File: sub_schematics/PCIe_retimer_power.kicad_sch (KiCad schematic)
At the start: 37 parts, among them M3 CSD15571Q2, M4 CSD13202Q2, U2 TPS62840YBGR, U3 TPS40303DRCR

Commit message: buck converter changes
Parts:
- removed Lz2: WB_SOURCE_INDUCTOR, symbol TI WEBENCH:root_0_Lz_TI WEBENCH
- removed Rz2: WB_SOURCE_RESISTOR, symbol TI WEBENCH:root_2_Rz_TI WEBENCH
- removed U2: TPS62840YBGR, symbol TI WEBENCH:root_0_U1_TI WEBENCH
- removed U3: TPS40303DRCR, symbol TI WEBENCH:root_0_U1_TI WEBENCH
- added Cb_inpflt1: C0805C106K8PACTU, symbol TI WEBENCH:root_1_Cb_inpflt_TI WEBENCH
- added Cf_inpflt1: C0805C106K8PACTU, symbol TI WEBENCH:root_1_Cf_inpflt_TI WEBENCH
- added Lf_inpflt1: 74479762122, symbol TI WEBENCH:root_0_Lf_inpflt_TI WEBENCH
- added Rd_inpflt1: CRCW04021R00FKED, symbol TI WEBENCH:root_1_Rd_inpflt_TI WEBENCH
- added U2: TPS62840YBGR, DSBGA6_1P4XP9_TEX, symbol step-down-converter-1.8V:TPS62840YBGR
- added U3: TPS40303DRCR, DRC10_2P4X1P65, symbol step-down-converter-1.17V:TPS40303DRCR
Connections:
- net 0: now also Cb_inpflt1.2 (-), Cf_inpflt1.2, U2.A1 (GND), U2.C2 (VSET), U3.11 (GND)
- net at Cout1.1, Iout1.1 (+), L1.1: now also U2.A2 (VOS)
- net at Ccomp5.1, Ccomp7.2, Rcomp3.2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: now also U3.5 (FB)
- net at Vin1.1 (+): now also Cf_inpflt1.1, Lf_inpflt1.1; no longer Cin1.1
- net at L1.2: now also U2.B2 (SW)
- net at M4.3 (Gate), Rs2.1: now also U3.9 (LDRV/OC)
- net at Cbyp2.1, Rpgood2.1: now also U3.10 (BP)
- net at Cf_inpflt2.1, Cf_inpflt_3.1, Lf_inpflt2.1: now also Vin3.1 (+)
- net at Cin3.1, Cvcc2.1, Lf_inpflt2.2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: now also U3.1 (VDD)
- net at Ccomp5.2, Ccomp6.2: now also U3.4 (COMP)
- net at M3.3 (Gate): now also U3.7 (HDRV)
- net at Cbst2.2, L3.2, M3.4 (Source)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: now also U3.8 (SW)
- net at Css2.1: now also U3.2 (EN/SS)
- net at Cbst2.1: now also U3.6 (BOOT)
- net at Rpgood2.2: now also U3.3 (PGOOD)
- new net: Cin1.1, Lf_inpflt1.2, Rd_inpflt1.1, U2.B1 (VIN), U2.C1 (EN)
- new net: Cb_inpflt1.1 (+), Rd_inpflt1.2
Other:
- moved on the sheet: Rpgood2

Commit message: buck converter
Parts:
- removed Cb_inpflt_3: UUD1V680MCL1GS, symbol TI WEBENCH:root_1_Cb_inpflt_2_TI WEBENCH
- removed Cf_inpflt_3: MSAST21GBB5106MTNA01, symbol TI WEBENCH:root_1_Cf_inpflt_2_TI WEBENCH
- removed Iout1: WB_CURRENT_LOAD, symbol TI WEBENCH:root_3_Iout_TI WEBENCH
- removed Rload2: WB_LOAD_RESISTOR, symbol TI WEBENCH:root_1_Rload_TI WEBENCH
- removed Vin1, Vin3: WB_BATTERY, symbol TI WEBENCH:root_3_Vin_TI WEBENCH
- added Cb_inpflt3: UUD1V680MCL1GS, symbol TI WEBENCH:root_1_Cb_inpflt_TI WEBENCH
- added Cf_inpflt3: MSAST21GBB5106MTNA01, symbol TI WEBENCH:root_1_Cf_inpflt_TI WEBENCH
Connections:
- net at M4.3 (Gate), Rs2.1: no longer U3.9 (LDRV/OC)
- net PWR.1_17V: now reaches Cout3.1, Cout_4.1, Cout_5.1, L3.1, Rcomp4.1, Rfbt2.1
- net at Cb_inpflt2.1 (+), Rd_inpflt2.2: now also Cb_inpflt3.1 (+)
- net PWR.1_8V: now reaches Cout1.1, L1.1, U2.A2 (VOS)
- net PWR.5V: now reaches Cf_inpflt1.1, Lf_inpflt1.1
- net PWR.5V: now also Cf_inpflt2.1, Lf_inpflt2.1, Cf_inpflt3.1
- net 0 renamed GND
- net GND: now also Cb_inpflt3.2 (-), Cf_inpflt3.2; no longer U2.A1 (GND)

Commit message: buck converter component
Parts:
- removed Cout3: C3216X5R0J107M160AB, symbol TI WEBENCH:root_1_Cout_TI WEBENCH
- removed Cout_4: C3216X5R0J107M160AB, symbol TI WEBENCH:root_1_Cout_2_TI WEBENCH
- removed Cout_5: C3216X5R0J107M160AB, symbol TI WEBENCH:root_1_Cout_3_TI WEBENCH
- removed M3: CSD15571Q2, symbol TI WEBENCH:root_0_M1_TI WEBENCH
- removed M4: CSD13202Q2, symbol TI WEBENCH:root_0_M2_TI WEBENCH
- added C17, C18, C19: C3216X5R0J107M160AB, step-down-converter-1.17V_sub_capacitor11:CAP_3216_TDK, symbol step-down-converter-1.17V_sub_capacitor11:C3216X5R0J107M160AB
- added U4: CSD13202Q2, step-down-converter-1.17V_sub_mosfet1:Q2_SON6_TEX, symbol step-down-converter-1.17V_sub_mosfet1:CSD13202Q2
- added U5: CSD15571Q2, step-down-converter-1.17V_sub_mosfet2:DQK6_TEX, symbol step-down-converter-1.17V_sub_mosfet2:CSD15571Q2
- C1: renamed from Cf_inpflt3; footprint (none) -> step-down-converter-1.17V_sub_capacitor1:CAP_MSAS21-G_TAY; symbol TI WEBENCH:root_1_Cf_inpflt_TI WEBENCH -> step-down-converter-1.17V_sub_capacitor1:MSAST21GBB5106MTNA01; ALTIUM_VALUE 10uF -> (none); MANUFACTURER NAME Taiyo Yuden -> (none); MANUFACTURER PART NUMBER MSAST21GBB5106MTNA01 -> (none); PACKAGEREFERENCE MSAST21GBB5106MTNA01 -> (none)
- C10: renamed from Cvcc2; footprint (none) -> step-down-converter-1.17V_sub_capacitor2:CAP_1005_TDK; symbol TI WEBENCH:root_1_Cvcc_TI WEBENCH -> step-down-converter-1.17V_sub_capacitor2:C1005X5R1E105K050BC; ALTIUM_VALUE 1uF -> (none); MANUFACTURER NAME TDK -> (none); MANUFACTURER PART NUMBER C1005X5R1E105K050BC -> (none); PACKAGEREFERENCE C1005X5R1E105K050BC -> (none)
- C11: renamed from Ccomp6; value C2012C0G1H153J085AA -> CGA4C2C0G1H472J060AA; footprint (none) -> step-down-converter-1.17V_sub_capacitor8:CAP_2012_TDK; symbol TI WEBENCH:root_3_Ccomp_TI WEBENCH -> step-down-converter-1.17V_sub_capacitor8:CGA4C2C0G1H472J060AA; ALTIUM_VALUE 15nF -> (none); MANUFACTURER NAME TDK -> (none); MANUFACTURER PART NUMBER C2012C0G1H153J085AA -> (none); PACKAGEREFERENCE C2012C0G1H153J085AA -> (none)
- C12: renamed from Css2; footprint (none) -> step-down-converter-1.17V_sub_capacitor3:CAP_0805P_AVX; symbol TI WEBENCH:root_1_Css_TI WEBENCH -> step-down-converter-1.17V_sub_capacitor3:08053A332JAT2A; ALTIUM_VALUE 3.3nF -> (none); MANUFACTURER NAME AVX -> (none); MANUFACTURER PART NUMBER 08053A332JAT2A -> (none); PACKAGEREFERENCE 08053A332JAT2A -> (none)
- C13: renamed from Cout1; footprint (none) -> step-down-converter-1.8V_sub_capacitors3:CAP_GRJ155R60J106ME11D_MUR; symbol TI WEBENCH:root_1_Cout_TI WEBENCH -> step-down-converter-1.8V_sub_capacitors3:GRJ155R60J106ME11D; ALTIUM_VALUE 10uF -> (none); MANUFACTURER NAME MuRata -> (none); MANUFACTURER PART NUMBER GRJ155R60J106ME11D -> (none); PACKAGEREFERENCE GRJ155R60J106ME11D -> (none)
- C14: renamed from Cbst2; footprint (none) -> step-down-converter-1.17V_sub_capacitor5:CAP_GRM_155_MUR; symbol TI WEBENCH:root_1_Cbst_TI WEBENCH -> step-down-converter-1.17V_sub_capacitor5:GRM155R71C104KA88D; ALTIUM_VALUE 100nF -> (none); MANUFACTURER NAME MuRata -> (none); MANUFACTURER PART NUMBER GRM155R71C104KA88D -> (none); PACKAGEREFERENCE GRM155R71C104KA88D -> (none)
- C15: renamed from Cbyp2; footprint (none) -> step-down-converter-1.17V_sub_capacitor10:CAPC17595_90N_KEM; symbol TI WEBENCH:root_1_Cbyp_TI WEBENCH -> step-down-converter-1.17V_sub_capacitor10:C0603C105Z8VACTU; ALTIUM_VALUE 1uF -> (none); MANUFACTURER NAME Kemet -> (none); MANUFACTURER PART NUMBER C0603C105Z8VACTU -> (none); PACKAGEREFERENCE C0603C105Z8VACTU -> (none)
- C16: renamed from Ccomp7; footprint (none) -> step-down-converter-1.17V_sub_capacitor8:CAP_2012_TDK; symbol TI WEBENCH:root_1_Ccomp3_TI WEBENCH -> step-down-converter-1.17V_sub_capacitor8:CGA4C2C0G1H472J060AA; ALTIUM_VALUE 4.7nF -> (none); MANUFACTURER NAME TDK -> (none); MANUFACTURER PART NUMBER CGA4C2C0G1H472J060AA -> (none); PACKAGEREFERENCE CGA4C2C0G1H472J060AA -> (none)
- C2: renamed from Cf_inpflt1; footprint (none) -> step-down-converter-1.8V_sub_capacitors:CAP_8PACTU; symbol TI WEBENCH:root_1_Cf_inpflt_TI WEBENCH -> step-down-converter-1.8V_sub_capacitors:C0805C106K8PACTU; ALTIUM_VALUE 10uF -> (none); MANUFACTURER NAME Kemet -> (none); MANUFACTURER PART NUMBER C0805C106K8PACTU -> (none); PACKAGEREFERENCE C0805C106K8PACTU -> (none)
- C3: renamed from Cf_inpflt2; footprint (none) -> step-down-converter-1.17V_sub_capacitor1:CAP_MSAS21-G_TAY; symbol TI WEBENCH:root_1_Cf_inpflt_TI WEBENCH -> step-down-converter-1.17V_sub_capacitor1:MSAST21GBB5106MTNA01; ALTIUM_VALUE 10uF -> (none); MANUFACTURER NAME Taiyo Yuden -> (none); MANUFACTURER PART NUMBER MSAST21GBB5106MTNA01 -> (none); PACKAGEREFERENCE MSAST21GBB5106MTNA01 -> (none)
- C4: renamed from Cb_inpflt3; value UUD1V680MCL1GS -> EEF-CT0J101R; footprint (none) -> step-down-converter-1.17V_sub_capacitor4:CAP_SP-CAP_CT_PAN; symbol TI WEBENCH:root_1_Cb_inpflt_TI WEBENCH -> step-down-converter-1.17V_sub_capacitor4:EEF-CT0J101R; ALTIUM_VALUE 68uF -> (none); MANUFACTURER NAME Nichicon -> (none); MANUFACTURER PART NUMBER UUD1V680MCL1GS -> (none); PACKAGEREFERENCE UUD1V680MCL1GS -> (none)
- C5: renamed from Cin1; footprint (none) -> step-down-converter-1.8V_sub_capacitors2:CAP_GRM15-5_MUR; symbol TI WEBENCH:root_1_Cin_TI WEBENCH -> step-down-converter-1.8V_sub_capacitors2:GRM155R60J475ME87D; ALTIUM_VALUE 4.7uF -> (none); MANUFACTURER NAME MuRata -> (none); MANUFACTURER PART NUMBER GRM155R60J475ME87D -> (none); PACKAGEREFERENCE GRM155R60J475ME87D -> (none)
- C6: renamed from Cb_inpflt2; value UUD1V680MCL1GS -> EEF-CT0J101R; footprint (none) -> step-down-converter-1.17V_sub_capacitor4:CAP_SP-CAP_CT_PAN; symbol TI WEBENCH:root_1_Cb_inpflt_TI WEBENCH -> step-down-converter-1.17V_sub_capacitor4:EEF-CT0J101R; ALTIUM_VALUE 68uF -> (none); MANUFACTURER NAME Nichicon -> (none); MANUFACTURER PART NUMBER UUD1V680MCL1GS -> (none); PACKAGEREFERENCE UUD1V680MCL1GS -> (none)
- C7: renamed from Ccomp5; footprint (none) -> step-down-converter-1.17V_sub_capacitor9:G-155_MUR; symbol TI WEBENCH:root_3_Ccomp2_TI WEBENCH -> step-down-converter-1.17V_sub_capacitor9:GRM1555C1H391JA01J; ALTIUM_VALUE 390pF -> (none); MANUFACTURER NAME MuRata -> (none); MANUFACTURER PART NUMBER GRM1555C1H391JA01J -> (none); PACKAGEREFERENCE GRM1555C1H391JA01J -> (none)
- C8: renamed from Cb_inpflt1; footprint (none) -> step-down-converter-1.8V_sub_capacitors:CAP_8PACTU; symbol TI WEBENCH:root_1_Cb_inpflt_TI WEBENCH -> step-down-converter-1.8V_sub_capacitors:C0805C106K8PACTU; ALTIUM_VALUE 10uF -> (none); MANUFACTURER NAME Kemet -> (none); MANUFACTURER PART NUMBER C0805C106K8PACTU -> (none); PACKAGEREFERENCE C0805C106K8PACTU -> (none)
- C9: renamed from Cin3; footprint (none) -> step-down-converter-1.17V_sub_capacitor7:G-32_MUR; symbol TI WEBENCH:root_1_Cin_TI WEBENCH -> step-down-converter-1.17V_sub_capacitor7:GRM32ER61C476KE15L; ALTIUM_VALUE 47uF -> (none); MANUFACTURER NAME MuRata -> (none); MANUFACTURER PART NUMBER GRM32ER61C476KE15L -> (none); PACKAGEREFERENCE GRM32ER61C476KE15L -> (none)
- L1: renamed from Lf_inpflt1; value 74479762122 -> 0603_H0.5_74479762122; footprint (none) -> step-down-converter-1.8V_sub_inductor:L_Wurth_WE-PMI-1008_H0.8; symbol TI WEBENCH:root_0_Lf_inpflt_TI WEBENCH -> step-down-converter-1.8V_sub_inductor:0603_H0.5_74479762122; ALTIUM_VALUE 220nH -> (none); Critical Parameter (none) -> 0.22 µH; H (mm) (none) -> 0.5; IR (mA) (none) -> 900; IR 2 (mA) (none) -> 1200; ISAT (mA) (none) -> 1300; L (µH) (none) -> 0.22; MANUFACTURER NAME Wurth Elektronik -> (none); MANUFACTURER PART NUMBER 74479762122 -> (none); Manufacturer (none) -> Wurth Elektronik; Manufacturer URL (none) -> https://www.we-online.com; Match Code (none) -> WE-PMI; Mounting Technology (none) -> SMT; PACKAGEREFERENCE 74479762122 -> (none); Part Number (none) -> 74479762122; Published Date (none) -> 20250214; RDC (mΩ) (none) -> 120.0; Size (none) -> 0603_H0.5; Type (none) -> Low Profile; W (mm) (none) -> 0.8; fres (MHz) (none) -> 250
- L2: renamed from Lf_inpflt2; footprint (none) -> step-down-converter-1.17V_sub_Inductor1:IND_DFE252012F-1R0M=P2_MUR; symbol TI WEBENCH:root_0_Lf_inpflt_TI WEBENCH -> step-down-converter-1.17V_sub_Inductor1:DFE252012F-1R0M=P2; ALTIUM_VALUE 1uH -> (none); MANUFACTURER NAME MuRata Toko -> (none); MANUFACTURER PART NUMBER DFE252012F-1R0M=P2 -> (none); PACKAGEREFERENCE DFE252012F-1R0M=P2 -> (none)
- L3: renamed from L1; value DFE201612E-2R2M=P2 -> 0603_H0.5_74479762122; footprint (none) -> step-down-converter-1.8V_sub_inductor:L_Wurth_WE-PMI-1008_H0.8; symbol TI WEBENCH:root_0_L1_TI WEBENCH -> step-down-converter-1.8V_sub_inductor:0603_H0.5_74479762122; ALTIUM_VALUE 2.2uH -> (none); Critical Parameter (none) -> 0.22 µH; H (mm) (none) -> 0.5; IR (mA) (none) -> 900; IR 2 (mA) (none) -> 1200; ISAT (mA) (none) -> 1300; L (µH) (none) -> 0.22; MANUFACTURER NAME MuRata -> (none); MANUFACTURER PART NUMBER DFE201612E-2R2M=P2 -> (none); Manufacturer (none) -> Wurth Elektronik; Manufacturer URL (none) -> https://www.we-online.com; Match Code (none) -> WE-PMI; Mounting Technology (none) -> SMT; PACKAGEREFERENCE DFE201612E-2R2M=P2 -> (none); Part Number (none) -> 74479762122; Published Date (none) -> 20250214; RDC (mΩ) (none) -> 120.0; Size (none) -> 0603_H0.5; Type (none) -> Low Profile; W (mm) (none) -> 0.8; fres (MHz) (none) -> 250
- L4: renamed from L3; value MSS1048-222NLB -> 5030_74439334022; footprint (none) -> step-down-converter-1.17V_sub_inductor2:L_Wurth_WE-XHMI-5030; symbol TI WEBENCH:root_0_L1_TI WEBENCH -> step-down-converter-1.17V_sub_inductor2:5030_74439334022; ALTIUM_VALUE 2.2uH -> (none); Critical Parameter (none) -> 2.2 µH; IRP,40K (A) (none) -> 10.3; ISAT,30% (A) (none) -> 12.8; L (µH) (none) -> 2.2; MANUFACTURER NAME Coilcraft -> (none); MANUFACTURER PART NUMBER MSS1048-222NLB -> (none); Manufacturer (none) -> Wurth Elektronik; Manufacturer URL (none) -> https://www.we-online.com; Match Code (none) -> WE-XHMI; Mounting Technology (none) -> SMT; PACKAGEREFERENCE MSS1048-222NLB -> (none); Part Number (none) -> 74439334022; Published Date (none) -> 20250613; RDC max. (mΩ) (none) -> 14.52; RDC typ. (mΩ) (none) -> 11.3; Size (none) -> 5030; fres (MHz) (none) -> 35
- R11: renamed from Rd_inpflt2; footprint (none) -> step-down-converter-1.17V_sub_resistor1:RC0603N_PAN; symbol TI WEBENCH:root_1_Rd_inpflt_TI WEBENCH -> step-down-converter-1.17V_sub_resistor1:ERJ-3RSFR10V; ALTIUM_VALUE 100m -> (none); MANUFACTURER NAME Panasonic -> (none); MANUFACTURER PART NUMBER ERJ-3RSFR10V -> (none); PACKAGEREFERENCE ERJ-3RSFR10V -> (none)
- R12: renamed from Rd_inpflt1; footprint (none) -> step-down-converter-1.8V_sub_inductor2:RC0402N_VIS; symbol TI WEBENCH:root_1_Rd_inpflt_TI WEBENCH -> step-down-converter-1.8V_sub_inductor2:CRCW04021R00FKED; ALTIUM_VALUE 1 -> (none); MANUFACTURER NAME Vishay-Dale -> (none); MANUFACTURER PART NUMBER CRCW04021R00FKED -> (none); PACKAGEREFERENCE CRCW04021R00FKED -> (none)
- R13: renamed from Rcomp3; footprint (none) -> step-down-converter-1.17V_sub_resistor2:RES_RT0805_YAG; symbol TI WEBENCH:root_1_Rcomp_TI WEBENCH -> step-down-converter-1.17V_sub_resistor2:RT0805BRD073K05L; ALTIUM_VALUE 3.05k -> (none); MANUFACTURER NAME Yageo -> (none); MANUFACTURER PART NUMBER RT0805BRD073K05L -> (none); PACKAGEREFERENCE RT0805BRD073K05L -> (none)
- R14: renamed from Rs2; footprint (none) -> step-down-converter-1.17V_sub_resistor8:RES_CRCW_0402; symbol TI WEBENCH:root_1_Rs_TI WEBENCH -> step-down-converter-1.17V_sub_resistor8:CRCW04023K74FKED; ALTIUM_VALUE 3.74k -> (none); MANUFACTURER NAME Vishay-Dale -> (none); MANUFACTURER PART NUMBER CRCW04023K74FKED -> (none); PACKAGEREFERENCE CRCW04023K74FKED -> (none)
- R15: renamed from Rpgood2; footprint (none) -> step-down-converter-1.17V_sub_resistor4:RES_CRCW_0402_VIS; symbol TI WEBENCH:root_3_Rpgood_TI WEBENCH -> step-down-converter-1.17V_sub_resistor4:CRCW0402100KFKED; ALTIUM_VALUE 100k -> (none); MANUFACTURER NAME Vishay-Dale -> (none); MANUFACTURER PART NUMBER CRCW0402100KFKED -> (none); PACKAGEREFERENCE CRCW0402100KFKED -> (none)
- R16: renamed from Rcomp4; footprint (none) -> step-down-converter-1.17V_sub_resistor7:RC0402N_VIS; symbol TI WEBENCH:root_1_Rcomp2_TI WEBENCH -> step-down-converter-1.17V_sub_resistor3:CRCW0402255RFKED; ALTIUM_VALUE 255 -> (none); MANUFACTURER NAME Vishay-Dale -> (none); MANUFACTURER PART NUMBER CRCW0402255RFKED -> (none); PACKAGEREFERENCE CRCW0402255RFKED -> (none)
- R17: renamed from Rfbt2; footprint (none) -> step-down-converter-1.17V_sub_resistor5:RES_CRCW_0402; symbol TI WEBENCH:root_1_Rfbt_TI WEBENCH -> step-down-converter-1.17V_sub_resistor6:CRCW040210K0FKED; ALTIUM_VALUE 10k -> (none); MANUFACTURER NAME Vishay-Dale -> (none); MANUFACTURER PART NUMBER CRCW040210K0FKED -> (none); PACKAGEREFERENCE CRCW040210K0FKED -> (none)
- R18: renamed from Rfbb2; footprint (none) -> step-down-converter-1.17V_sub_resistor6:RES_CRCW_0402; symbol TI WEBENCH:root_1_Rfbb_TI WEBENCH -> step-down-converter-1.17V_sub_resistor5:CRCW040210K5FKED; ALTIUM_VALUE 10.5k -> (none); MANUFACTURER NAME Vishay-Dale -> (none); MANUFACTURER PART NUMBER CRCW040210K5FKED -> (none); PACKAGEREFERENCE CRCW040210K5FKED -> (none)
- U2: footprint DSBGA6_1P4XP9_TEX -> step-down-converter-1.8V:DSBGA6_1P4XP9_TEX
- U3: footprint DRC10_2P4X1P65 -> step-down-converter-1.17V:DRC10_2P4X1P65
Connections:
- net GND: now also U2.A1 (GND), C17.2, C18.2, C19.2, U4.4 (S), U4.7 (S), U5.7 (EPAD), U5.8 (EPAD)
- net PWR.1_17V: now also R17.2, C17.1, C18.1, C19.1; no longer R17.1
- net PWR.1_8V: now also L3.2; no longer L3.1
- net PWR.5V: now also L2.2; no longer L2.1
- net at C5.1, L1.2, U2.B1 (VIN)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: now also R12.2; no longer R12.1
- net at C14.2, L4.2, U3.8 (SW): now also U4.1 (D), U4.2 (D), U4.5 (D), U4.6 (D), U4.8 (D), U5.4 (S)
- net at R14.1: now also U3.9 (LDRV/OC), U4.3 (G)
- net at C10.1, C9.1, U3.1 (VDD): now also L2.1, R11.2, U5.1 (D), U5.2 (D), U5.5 (D), U5.6 (D); no longer L2.2, R11.1
- net at U3.7 (HDRV): now also U5.3 (G)
- net at C4.1, C6.1: now also R11.1; no longer R11.2
- net at C16.2, R13.2, R18.1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: now also C7.2, R17.1; no longer C7.1, R17.2
- net at C11.2, U3.4 (COMP): now also C7.1; no longer C7.2
- net at C15.1, U3.10 (BP): now also R15.2; no longer R15.1
- net at U3.3 (PGOOD): now also R15.1; no longer R15.2
- net at U2.B2 (SW): now also L3.1; no longer L3.2
- net at C8.1: now also R12.1; no longer R12.2
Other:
- moved on the sheet: C1, C10, C11, C12, C14, C15, C16, C2, C3, C4, C6, C7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

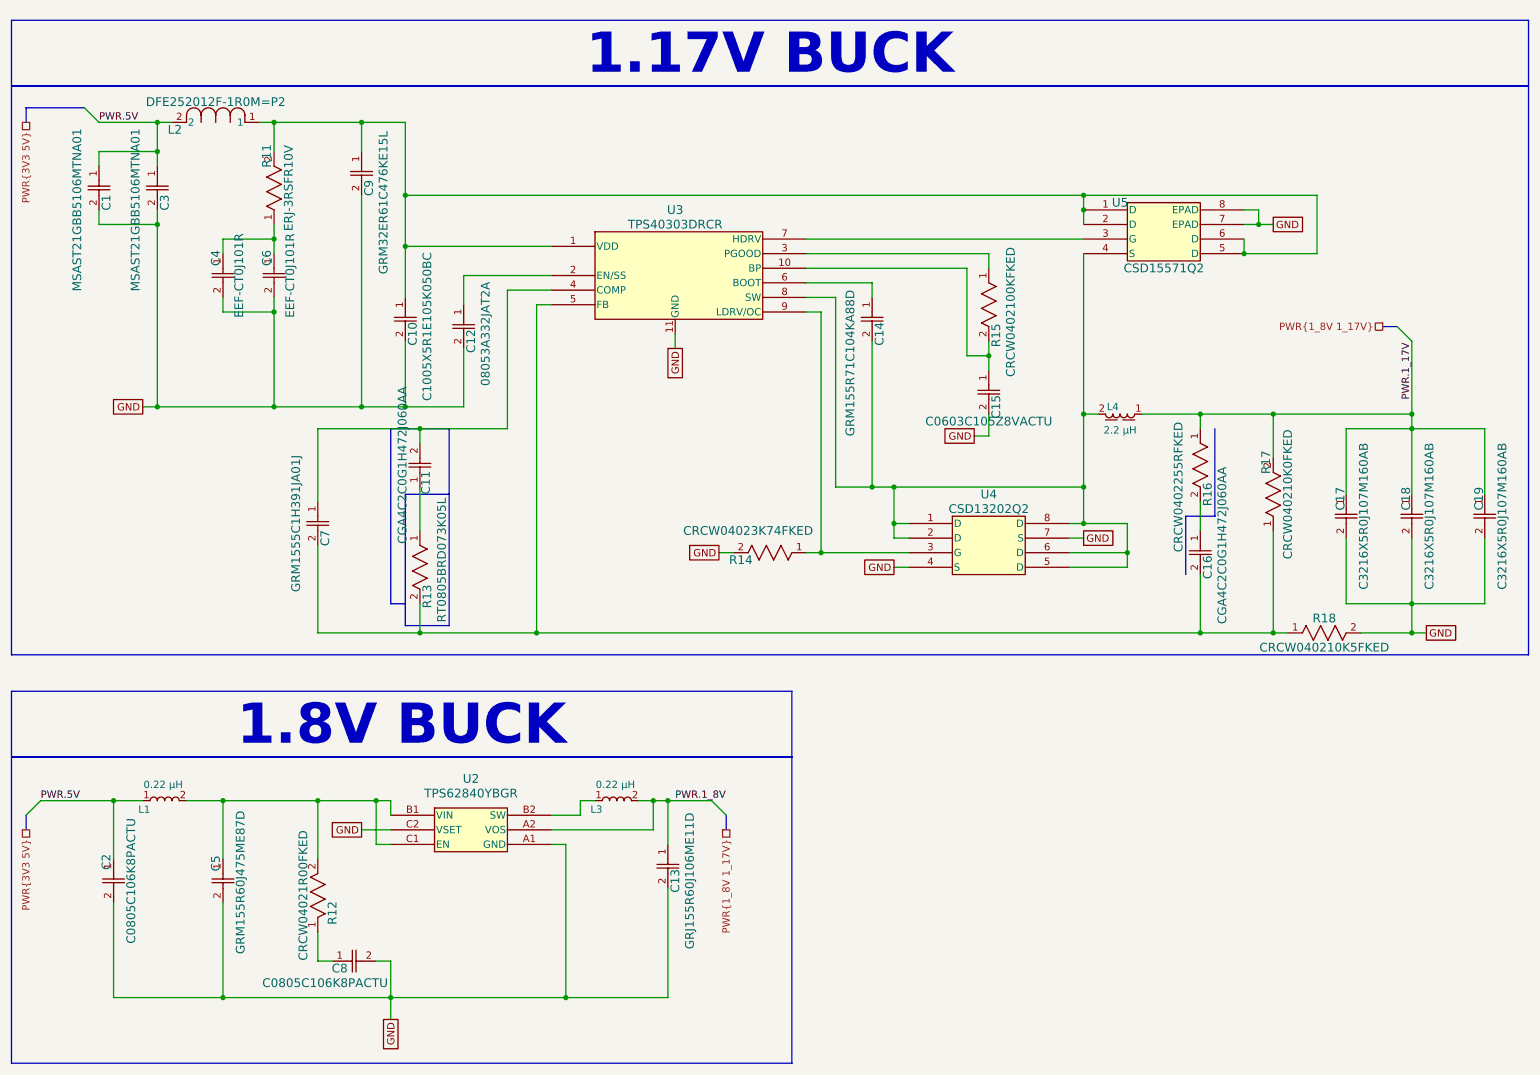
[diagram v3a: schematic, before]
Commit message: Schematics revamped
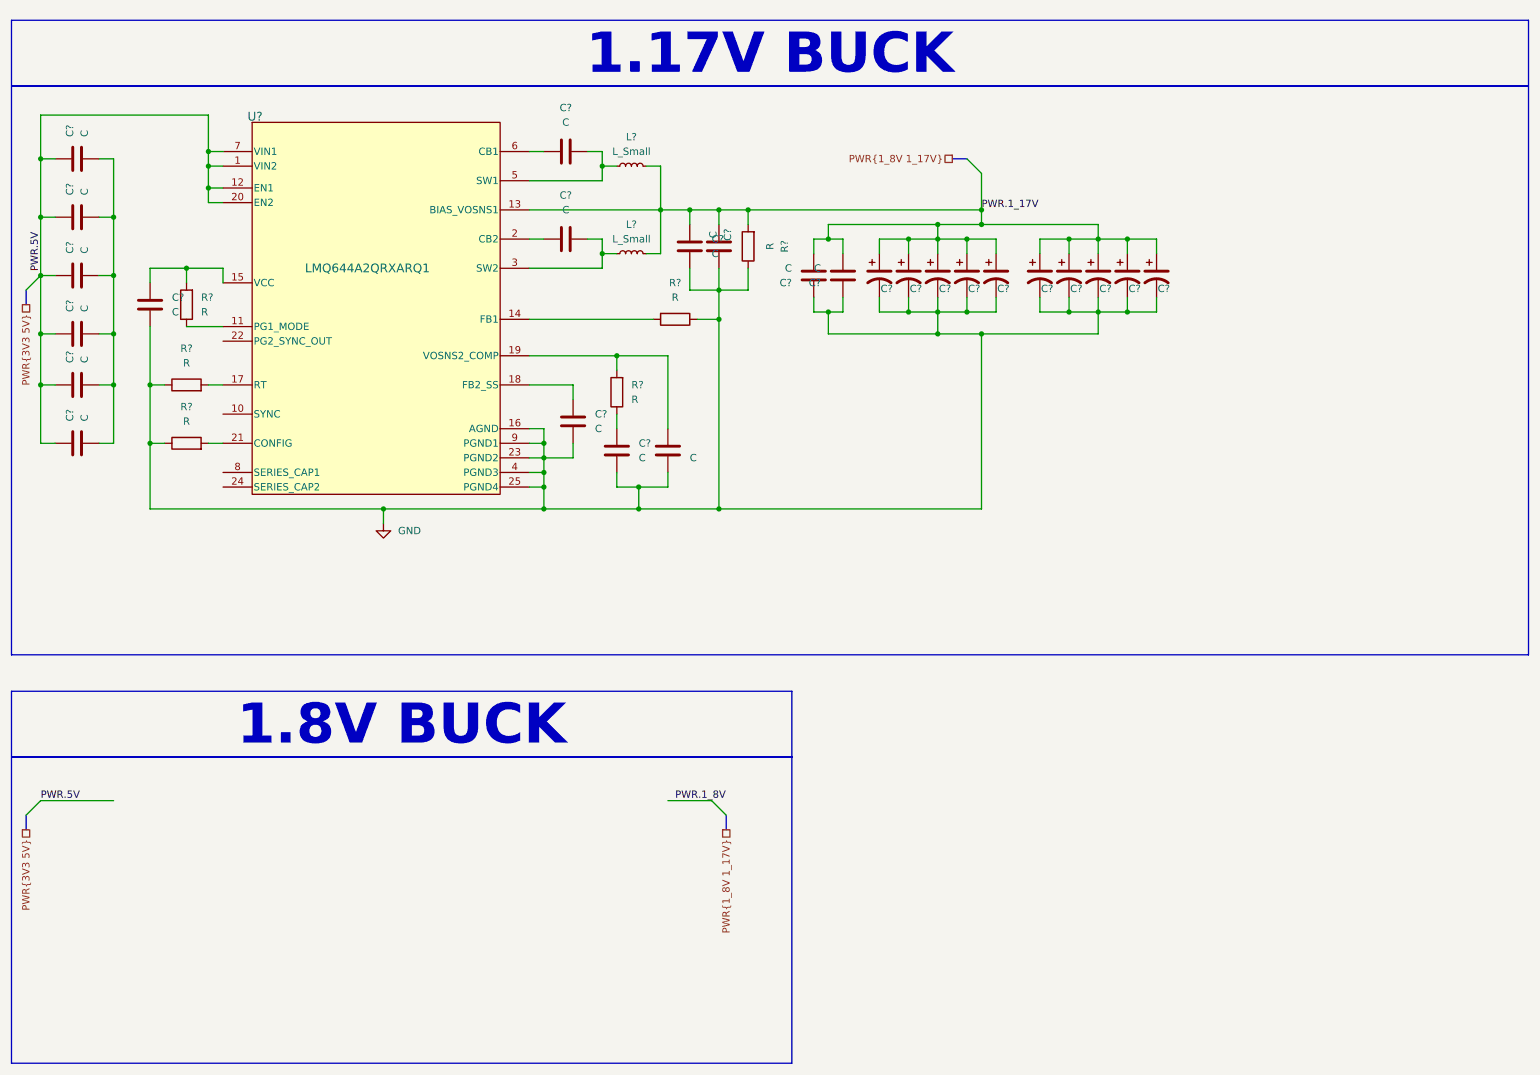
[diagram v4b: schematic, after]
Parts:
- removed C1, C3: MSAST21GBB5106MTNA01, step-down-converter-1.17V_sub_capacitor1:CAP_MSAS21-G_TAY, symbol step-down-converter-1.17V_sub_capacitor1:MSAST21GBB5106MTNA01
- removed C10: C1005X5R1E105K050BC, step-down-converter-1.17V_sub_capacitor2:CAP_1005_TDK, symbol step-down-converter-1.17V_sub_capacitor2:C1005X5R1E105K050BC
- removed C11, C16: CGA4C2C0G1H472J060AA, step-down-converter-1.17V_sub_capacitor8:CAP_2012_TDK, symbol step-down-converter-1.17V_sub_capacitor8:CGA4C2C0G1H472J060AA
- removed C12: 08053A332JAT2A, step-down-converter-1.17V_sub_capacitor3:CAP_0805P_AVX, symbol step-down-converter-1.17V_sub_capacitor3:08053A332JAT2A
- removed C13: GRJ155R60J106ME11D, step-down-converter-1.8V_sub_capacitors3:CAP_GRJ155R60J106ME11D_MUR, symbol step-down-converter-1.8V_sub_capacitors3:GRJ155R60J106ME11D
- removed C14: GRM155R71C104KA88D, step-down-converter-1.17V_sub_capacitor5:CAP_GRM_155_MUR, symbol step-down-converter-1.17V_sub_capacitor5:GRM155R71C104KA88D
- removed C15: C0603C105Z8VACTU, step-down-converter-1.17V_sub_capacitor10:CAPC17595_90N_KEM, symbol step-down-converter-1.17V_sub_capacitor10:C0603C105Z8VACTU
- removed C17, C18, C19: C3216X5R0J107M160AB, step-down-converter-1.17V_sub_capacitor11:CAP_3216_TDK, symbol step-down-converter-1.17V_sub_capacitor11:C3216X5R0J107M160AB
- removed C2, C8: C0805C106K8PACTU, step-down-converter-1.8V_sub_capacitors:CAP_8PACTU, symbol step-down-converter-1.8V_sub_capacitors:C0805C106K8PACTU
- removed C4, C6: EEF-CT0J101R, step-down-converter-1.17V_sub_capacitor4:CAP_SP-CAP_CT_PAN, symbol step-down-converter-1.17V_sub_capacitor4:EEF-CT0J101R
- removed C5: GRM155R60J475ME87D, step-down-converter-1.8V_sub_capacitors2:CAP_GRM15-5_MUR, symbol step-down-converter-1.8V_sub_capacitors2:GRM155R60J475ME87D
- removed C7: GRM1555C1H391JA01J, step-down-converter-1.17V_sub_capacitor9:G-155_MUR, symbol step-down-converter-1.17V_sub_capacitor9:GRM1555C1H391JA01J
- removed C9: GRM32ER61C476KE15L, step-down-converter-1.17V_sub_capacitor7:G-32_MUR, symbol step-down-converter-1.17V_sub_capacitor7:GRM32ER61C476KE15L
- removed L1, L3: 0603_H0.5_74479762122, step-down-converter-1.8V_sub_inductor:L_Wurth_WE-PMI-1008_H0.8, symbol step-down-converter-1.8V_sub_inductor:0603_H0.5_74479762122
- removed L2: DFE252012F-1R0M=P2, step-down-converter-1.17V_sub_Inductor1:IND_DFE252012F-1R0M=P2_MUR, symbol step-down-converter-1.17V_sub_Inductor1:DFE252012F-1R0M=P2
- removed L4: 5030_74439334022, step-down-converter-1.17V_sub_inductor2:L_Wurth_WE-XHMI-5030, symbol step-down-converter-1.17V_sub_inductor2:5030_74439334022
- removed R11: ERJ-3RSFR10V, step-down-converter-1.17V_sub_resistor1:RC0603N_PAN, symbol step-down-converter-1.17V_sub_resistor1:ERJ-3RSFR10V
- removed R12: CRCW04021R00FKED, step-down-converter-1.8V_sub_inductor2:RC0402N_VIS, symbol step-down-converter-1.8V_sub_inductor2:CRCW04021R00FKED
- removed R13: RT0805BRD073K05L, step-down-converter-1.17V_sub_resistor2:RES_RT0805_YAG, symbol step-down-converter-1.17V_sub_resistor2:RT0805BRD073K05L
- removed R14: CRCW04023K74FKED, step-down-converter-1.17V_sub_resistor8:RES_CRCW_0402, symbol step-down-converter-1.17V_sub_resistor8:CRCW04023K74FKED
- removed R15: CRCW0402100KFKED, step-down-converter-1.17V_sub_resistor4:RES_CRCW_0402_VIS, symbol step-down-converter-1.17V_sub_resistor4:CRCW0402100KFKED
- removed R16: CRCW0402255RFKED, step-down-converter-1.17V_sub_resistor7:RC0402N_VIS, symbol step-down-converter-1.17V_sub_resistor3:CRCW0402255RFKED
- removed R17: CRCW040210K0FKED, step-down-converter-1.17V_sub_resistor5:RES_CRCW_0402, symbol step-down-converter-1.17V_sub_resistor6:CRCW040210K0FKED
- removed R18: CRCW040210K5FKED, step-down-converter-1.17V_sub_resistor6:RES_CRCW_0402, symbol step-down-converter-1.17V_sub_resistor5:CRCW040210K5FKED
- removed U2: TPS62840YBGR, step-down-converter-1.8V:DSBGA6_1P4XP9_TEX, symbol step-down-converter-1.8V:TPS62840YBGR
- removed U3: TPS40303DRCR, step-down-converter-1.17V:DRC10_2P4X1P65, symbol step-down-converter-1.17V:TPS40303DRCR
- removed U4: CSD13202Q2, step-down-converter-1.17V_sub_mosfet1:Q2_SON6_TEX, symbol step-down-converter-1.17V_sub_mosfet1:CSD13202Q2
- removed U5: CSD15571Q2, step-down-converter-1.17V_sub_mosfet2:DQK6_TEX, symbol step-down-converter-1.17V_sub_mosfet2:CSD15571Q2
- added C? (x16): C, symbol Device:C
- added C? (x10): C_Polarized_US, symbol Device:C_Polarized_US
- added L? (x2): L_Small, symbol Device:L_Small
- added R? (x6): R, symbol Device:R
- added U?: LMQ644A2QRXARQ1, step-down-converter-1.17V:RXA0024A-MFG, symbol step-down-converter-1.17V:LMQ644A2QRXARQ1
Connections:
- net GND: now also C?.1, C?.1, C?.1, C?.1, C?.2, C?.2, C?.2, C?.2, C?.2, C?.2, C?.2, C?.2, C?.2, C?.2, C?.2, C?.2, C?.2, C?.2, R?.1, R?.1, R?.1, R?.1, U?.16 (AGND), U?.23 (PGND2), U?.25 (PGND4), U?.4 (PGND3), U?.9 (PGND1)
- net PWR.1_17V: now also C?.1, C?.1, C?.1, C?.1, C?.1, C?.1, C?.1, C?.1, C?.1, C?.1, C?.1, C?.1, C?.1, C?.1, L?.2, L?.2, R?.2, U?.13 (BIAS_VOSNS1)
- net PWR.5V: now also C?.1, C?.1, C?.1, C?.1, C?.1, C?.1, U?.1 (VIN2), U?.12 (EN1), U?.20 (EN2), U?.7 (VIN1)
- new net: C?.2, C?.2, C?.2, C?.2, C?.2, C?.2
- new net: C?.2, U?.18 (FB2_SS)
- new net: R?.1, U?.11 (PG1_MODE)
- new net: R?.2, U?.14 (FB1)
- new net: C?.2, R?.2, U?.15 (VCC)
- new net: R?.2, U?.17 (RT)
- new net: C?.2, R?.2, U?.19 (VOSNS2_COMP)
- new net: C?.1, U?.2 (CB2)
- new net: R?.2, U?.21 (CONFIG)
- new net: C?.2, L?.1, U?.3 (SW2)
- new net: C?.2, L?.1, U?.5 (SW1)
- new net: C?.1, U?.6 (CB1)
- new net: C?.2, R?.1
